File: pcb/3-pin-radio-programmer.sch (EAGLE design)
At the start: 14 parts, among them U1 ATTINY85-20SU

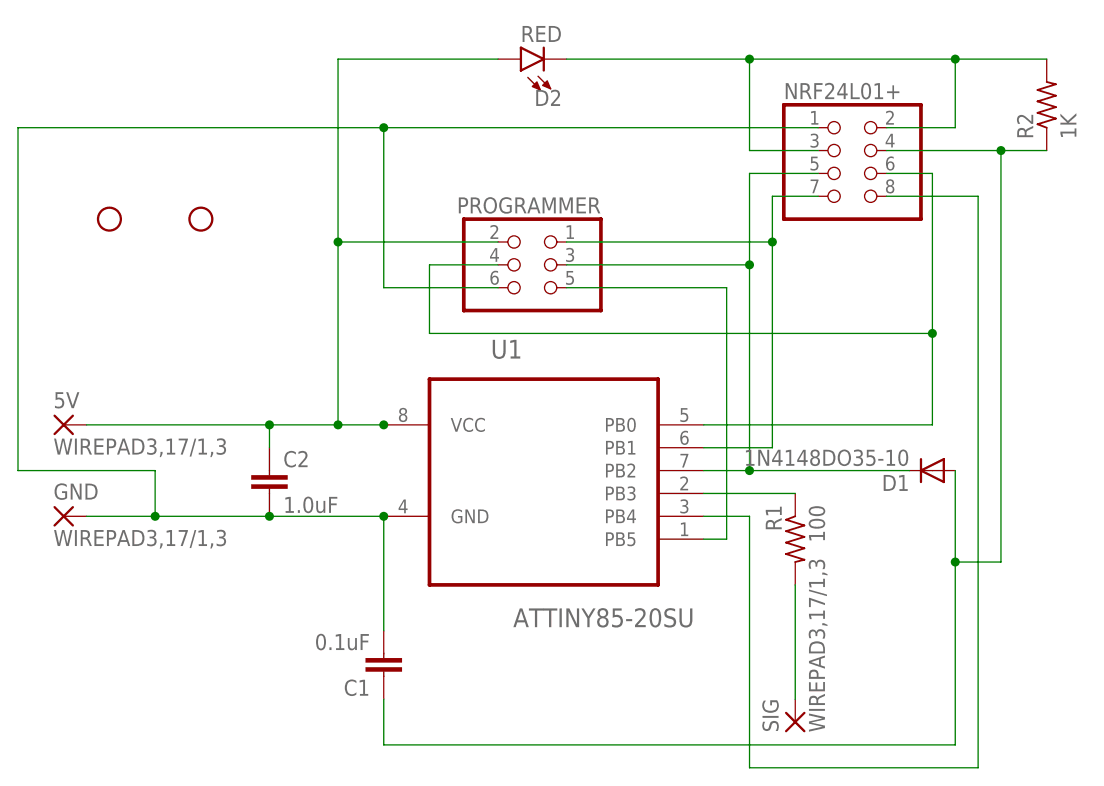
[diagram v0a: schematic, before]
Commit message: Adding pull up on reset pin
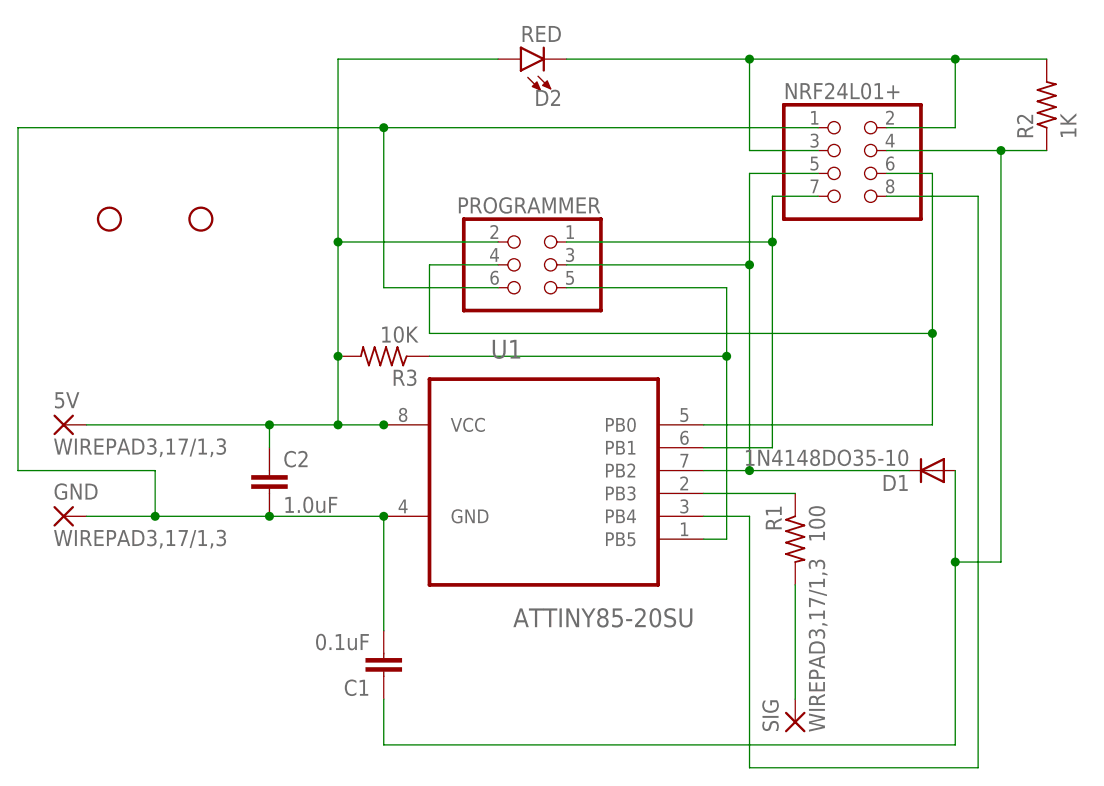
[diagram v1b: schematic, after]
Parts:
- added R3: 10K, rcl:R-US_R0805
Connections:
- net N$11: now also R3.2
- net N$13: now also R3.1
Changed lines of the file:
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@@
 <part name="H1" library="SparkFun-Hardware" deviceset="STAND-OFF" device=""/>
 <part name="H2" library="SparkFun-Hardware" deviceset="STAND-OFF" device=""/>
+<part name="R3" library="rcl" deviceset="R-US_" device="R0805" value="10K"/>
 </parts>
 <sheets>
@@
 <instance part="H1" gate="G$1" x="10.16" y="91.44"/>
 <instance part="H2" gate="G$1" x="20.32" y="91.44"/>
+<instance part="R3" gate="G$1" x="40.64" y="76.2" rot="R180"/>
 </instances>
 <busses>
@@
 <wire x1="35.56" y1="109.22" x2="35.56" y2="88.9" width="0.1524" layer="91"/>
 <pinref part="U1" gate="A" pin="VCC"/>
-<wire x1="35.56" y1="88.9" x2="35.56" y2="68.58" width="0.1524" layer="91"/>
+<wire x1="35.56" y1="88.9" x2="35.56" y2="76.2" width="0.1524" layer="91"/>
+<wire x1="35.56" y1="76.2" x2="35.56" y2="68.58" width="0.1524" layer="91"/>
 <wire x1="40.64" y1="68.58" x2="35.56" y2="68.58" width="0.1524" layer="91"/>
 <junction x="35.56" y="68.58"/>
@@
 <wire x1="53.34" y1="88.9" x2="35.56" y2="88.9" width="0.1524" layer="91"/>
 <junction x="35.56" y="88.9"/>
+<pinref part="R3" gate="G$1" pin="2"/>
+<junction x="35.56" y="76.2"/>
 </segment>
 </net>
@@
 <pinref part="PROGRAMMER" gate="A" pin="5"/>
 <wire x1="60.96" y1="83.82" x2="78.74" y2="83.82" width="0.1524" layer="91"/>
-<wire x1="78.74" y1="83.82" x2="78.74" y2="55.88" width="0.1524" layer="91"/>
+<wire x1="78.74" y1="83.82" x2="78.74" y2="76.2" width="0.1524" layer="91"/>
 <pinref part="U1" gate="A" pin="PB5"/>
+<wire x1="78.74" y1="76.2" x2="78.74" y2="55.88" width="0.1524" layer="91"/>
 <wire x1="78.74" y1="55.88" x2="76.2" y2="55.88" width="0.1524" layer="91"/>
+<pinref part="R3" gate="G$1" pin="1"/>
+<wire x1="45.72" y1="76.2" x2="78.74" y2="76.2" width="0.1524" layer="91"/>
+<junction x="78.74" y="76.2"/>
 </segment>
 </net>
